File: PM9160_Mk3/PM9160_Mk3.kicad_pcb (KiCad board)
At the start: 2 copper layers, 100 x 40 mm, 87 parts, among them J1 Conn_Coaxial, U1 BGA2869, U2 ATtiny416-M, U3 SY100EL33L, U4 SY100EL33L, U5 LM317L_TO92

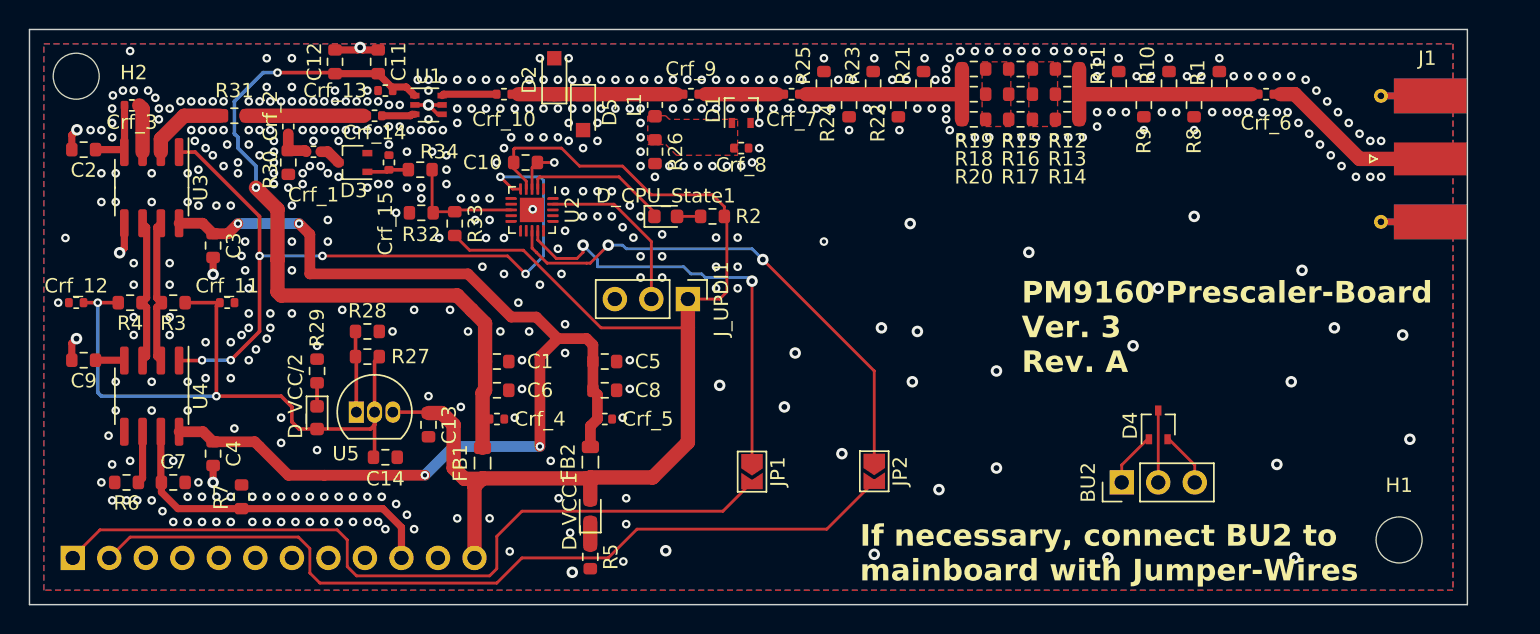
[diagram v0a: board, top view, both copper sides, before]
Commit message: CPU change and fixed via clearances
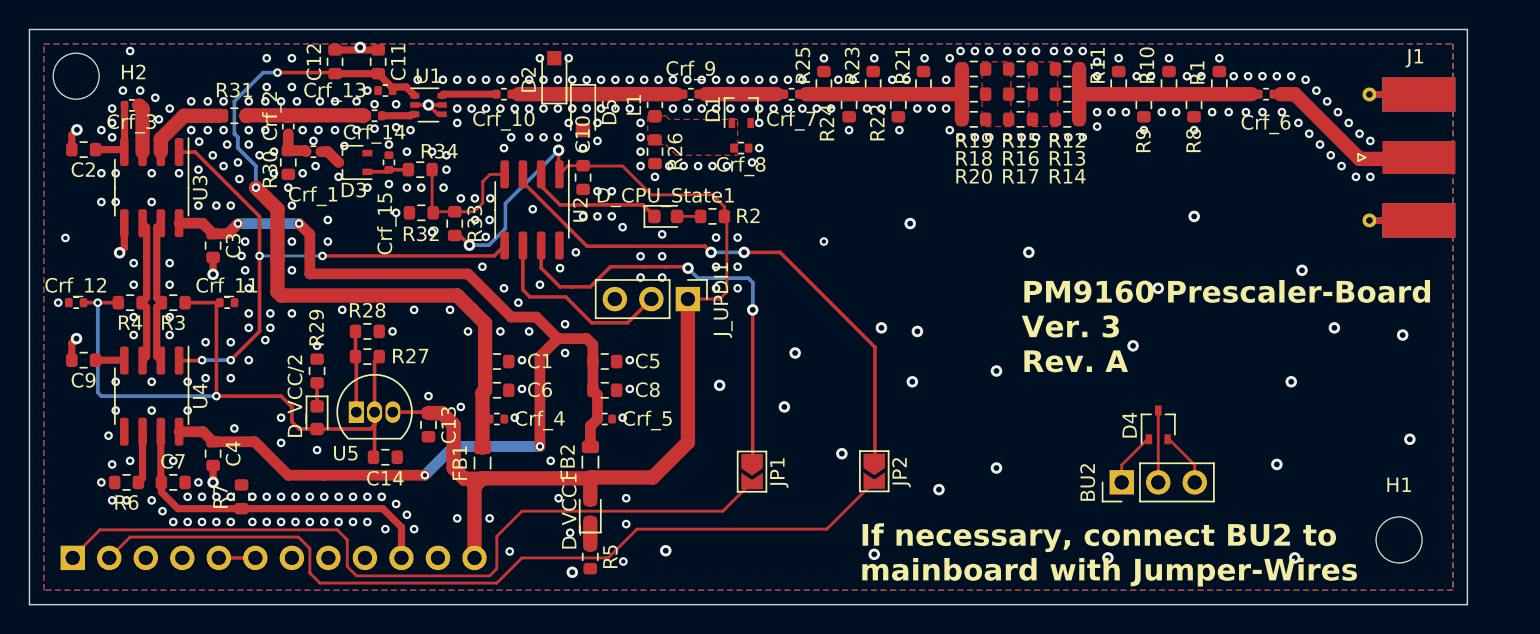
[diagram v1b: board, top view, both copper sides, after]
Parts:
- U2: value ATtiny416-M -> ATtiny202-SS; footprint Package_DFN_QFN:VQFN-20-1EP_3x3mm_P0.4mm_EP1.7x1.7mm -> Package_SO:SOIC-8_3.9x4.9mm_P1.27mm
- moved C10 4.14 mm to (148.5, 100.3), turned to 90 degrees
- moved J1 0.81 mm to (204.9, 98.9)
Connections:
- U2 pad 1: unconnected-(U2-PA2-Pad1) -> +5V
- U2 pad 3: GND -> Net-(JP2-A)
- U2 pad 4: +5V -> RF_DETECT
- U2 pad 6: unconnected-(U2-PA5-Pad6) -> UPDI
- U2 pad 7: unconnected-(U2-PA6-Pad7) -> Net-(JP1-A)
- U2 pad 8: RF_DETECT -> GND
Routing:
- net RF_RESET: track 52.8 -> 39.2 mm, vias 6 -> 4
- net +5V: track 89.8 -> 77.3 mm, vias 0 -> 2
- net GND: track 17.3 -> 14.2 mm, vias 462 -> 404
- net Net-(BU7-Pin_5): track 0.00 -> 2.54 mm
- net Net-(JP2-A): track 35.8 -> 37.7 mm
- net UPDI: track 11.9 -> 13.7 mm
- net RF_DETECT: track 8.54 -> 9.99 mm
- net CPU_STATE: track 10.2 -> 9.56 mm
